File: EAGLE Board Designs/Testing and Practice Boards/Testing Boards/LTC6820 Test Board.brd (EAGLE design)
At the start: 77.5 x 41.8 mm, 15 parts, among them J4 CONNECTOR-2_MF_T_V_, T1 TRANSFORMER_HM2112ZNLT_AIRGAP, U1 LTC6820

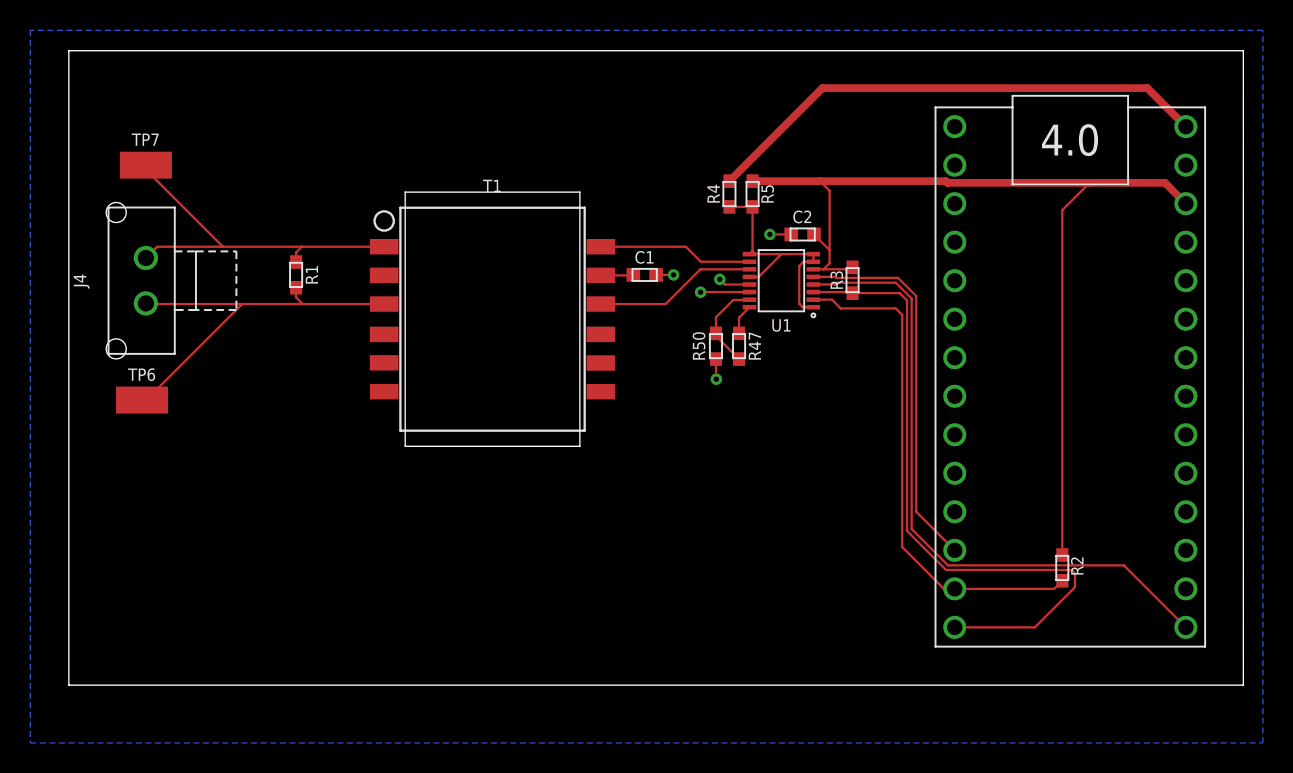
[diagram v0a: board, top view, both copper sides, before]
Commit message: update board for on campus drc
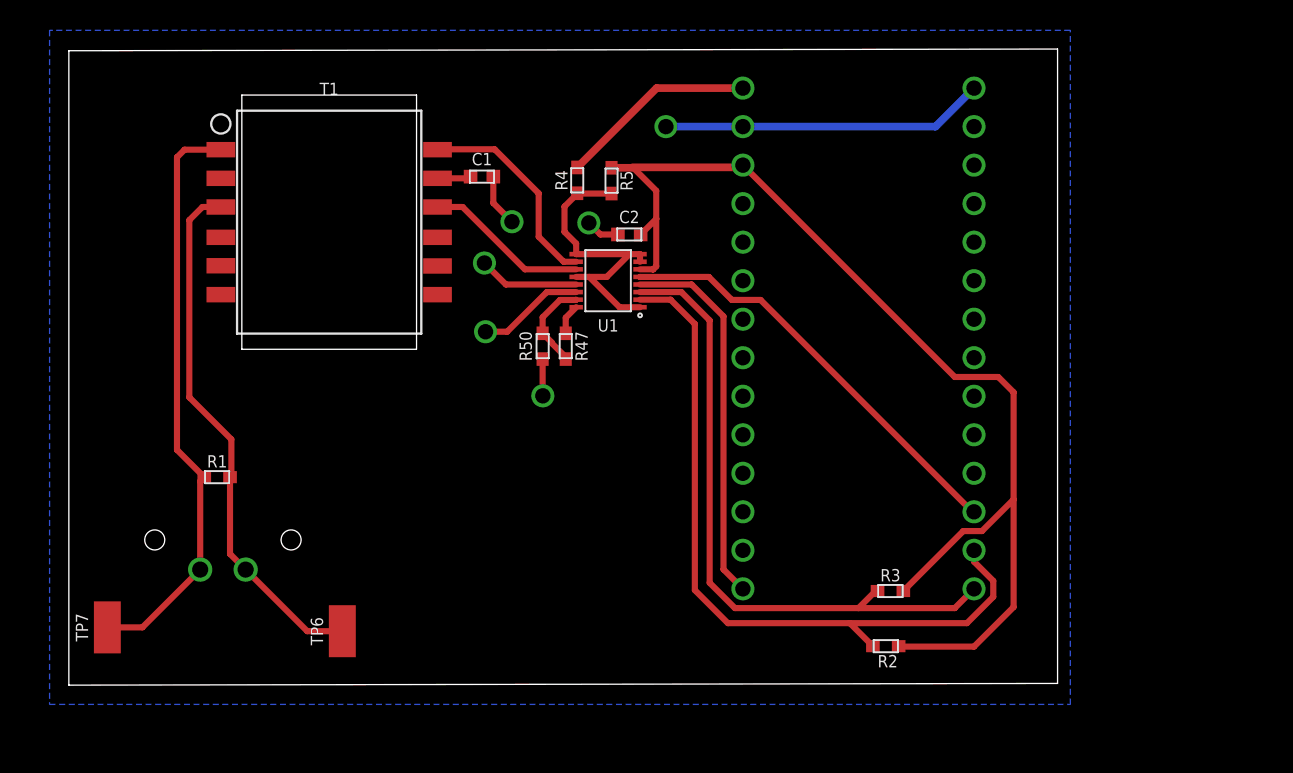
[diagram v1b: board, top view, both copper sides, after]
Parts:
- moved TP7 30.6 mm to (2.54, 3.81), turned to 90 degrees
- moved A1 29.3 mm to (44.5, 39.4), flipped to the bottom
- moved R3 20.6 mm to (54.2, 6.21), turned to 0 degrees
- moved TP6 20.2 mm to (18.0, 3.56), turned to 90 degrees
- moved J4 19.7 mm to (10.2, 7.62), flipped to the bottom, turned to 180 degrees
- moved R1 14.3 mm to (9.78, 13.7), turned to 0 degrees
- moved R2 12.7 mm to (53.9, 2.57), turned to 0 degrees
- moved C1 12.5 mm to (27.2, 33.5)
- moved T1 12.5 mm to (17.2, 30.5)
- moved C2 11.4 mm to (37.0, 29.7)
- moved R47 11.4 mm to (32.8, 22.4)
- moved U1 11.4 mm to (35.6, 26.7)
- moved R50 11.4 mm to (31.2, 22.4)
- moved R4 10.1 mm to (33.5, 33.3)
- moved R5 9.34 mm to (35.8, 33.3)
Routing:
- net GND: track 9.24 -> 43.2 mm, vias 5 -> 6
- net +5V: track 33.7 -> 13.1 mm
- net N$2: track 42.9 -> 24.9 mm
- net N$4: track 33.5 -> 48.9 mm
- net IM: track 24.7 -> 38.8 mm
- net +3V3: track 64.8 -> 75.2 mm
- net IP: track 26.2 -> 35.2 mm
- net N$38: track 10.2 -> 13.9 mm
- net N$5: track 25.1 -> 28.4 mm
- net N$6: track 16.7 -> 20.0 mm
- net N$3: track 44.3 -> 43.0 mm
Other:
- board size 77.5 x 41.8 mm -> 65.2 x 41.9 mm
